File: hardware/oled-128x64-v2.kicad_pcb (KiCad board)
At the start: 2 copper layers, 40 x 40 mm, 34 parts, among them P1 CON-SENSOR2, P2 DEBUG, P3 BOOT, U1 XMC130024, U3 OLED013, U4 DRILL, U5 DRILL, U6 DRILL, U7 DRILL

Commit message: add text
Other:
- board text added: "Copyright Tinkerforge GmbH 2018. This documentation describes Open Hardware and is licensed under the CERN OHL v. 1.1. You may redistribute and modify this documentation under the terms of the CERN OHL v.1.1. (http://ohwr.org/cernohl). This documentation is distributed WITHOUT ANY EXPRESS OR IMPLIED WARRANTY, INCLUDING OF MERCHANTABILITY, SATISFACTORY QUALITY AND FITNESS FOR A PARTICULAR PURPOSE.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"
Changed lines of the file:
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@@
     (area 133.244999 120.744999 174.955001 162.455001)
     (thickness 1.6)
-    (drawings 24)
+    (drawings 25)
     (tracks 303)
     (zones 0)
@@
       (xy 1.301301 -2.715081) (xy 1.302426 -2.714986)) (layer F.SilkS) (width 0.01))
   )
+  (gr_text "Copyright Tinkerforge GmbH 2018.\nThis documentation describes Open Hardware and is licensed under the\nCERN OHL v. 1.1.\nYou may redistribute and modify this documentation under the terms of the\nCERN OHL v.1.1. (http://ohwr.org/cernohl). This documentation is distributed\nWITHOUT ANY EXPRESS OR IMPLIED WARRANTY, INCLUDING OF\nMERCHANTABILITY, SATISFACTORY QUALITY AND FITNESS FOR A\nPARTICULAR PURPOSE. Please see the CERN OHL v.1.1 for applicable\nconditions\n" (at 233.7 144.2) (layer Cmts.User)
+    (effects (font (size 1.5 1.5) (thickness 0.3048)))
+  )
   (gr_text Status (at 163.28 122.65) (layer F.SilkS)

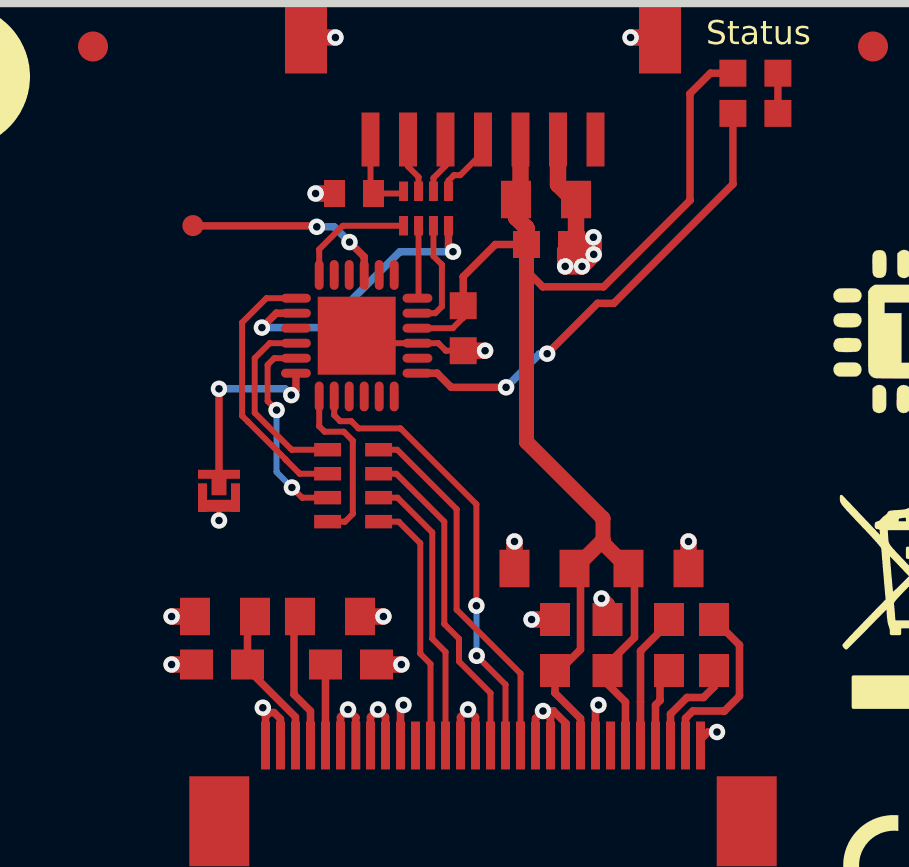
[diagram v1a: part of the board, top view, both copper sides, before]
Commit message: Change footprint to x0402F/x0603F
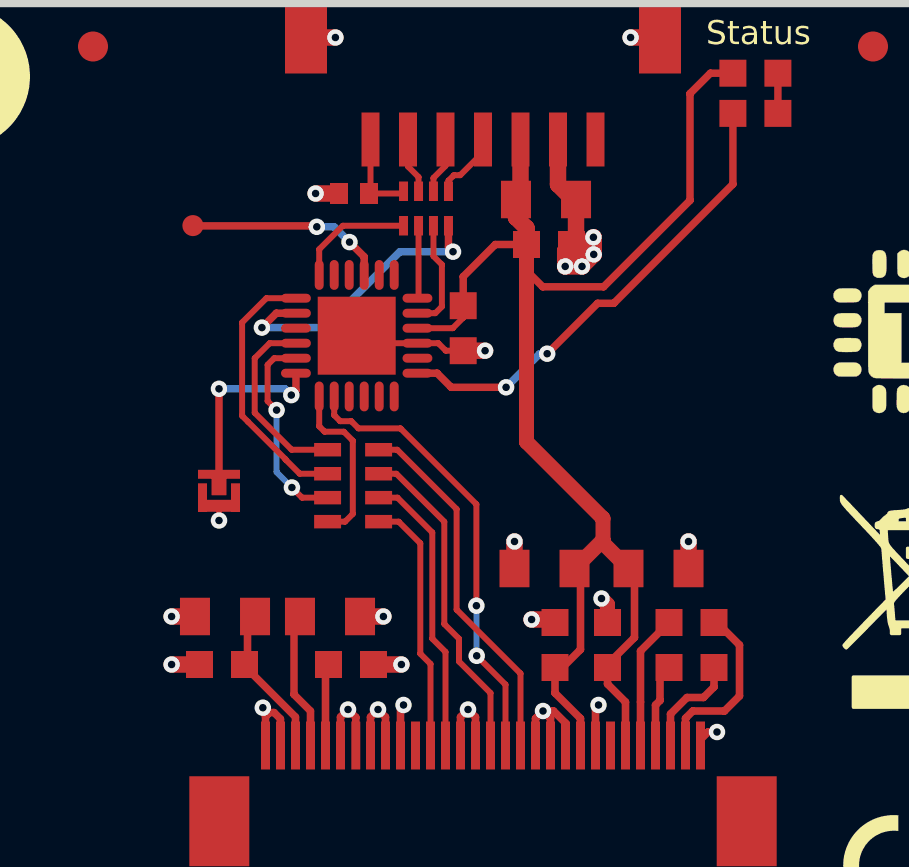
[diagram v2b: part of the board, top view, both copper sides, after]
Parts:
- C1: footprint kicad-libraries:C0402E -> kicad-libraries:C0402F
- C10, C11, C4, C6, C8: footprint kicad-libraries:C0603E -> kicad-libraries:C0603F
- R1: footprint kicad-libraries:R0603E -> kicad-libraries:R0603F
